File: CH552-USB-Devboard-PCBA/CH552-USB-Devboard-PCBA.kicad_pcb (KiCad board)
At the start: 2 copper layers, 22 x 48.1 mm, 47 parts, among them J1 Conn_01x11_Male, J2 Conn_01x11_Male, J3 USB_C_Receptacle, J4 USB_C_Receptacle, SW1 SW_Push, SW2 SW_Push, U2 CH552G, U3 TPS7A4101DGNT

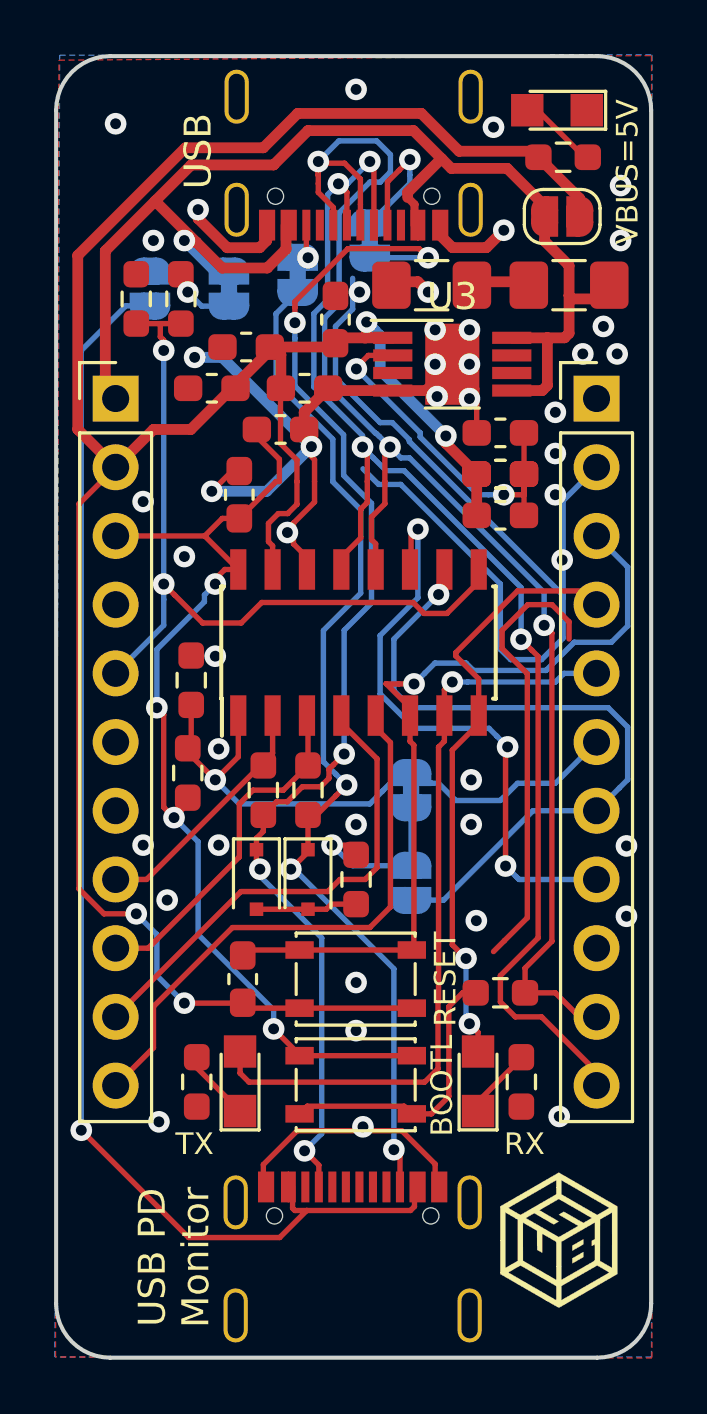
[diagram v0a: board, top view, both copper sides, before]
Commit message: create variant for PCBA
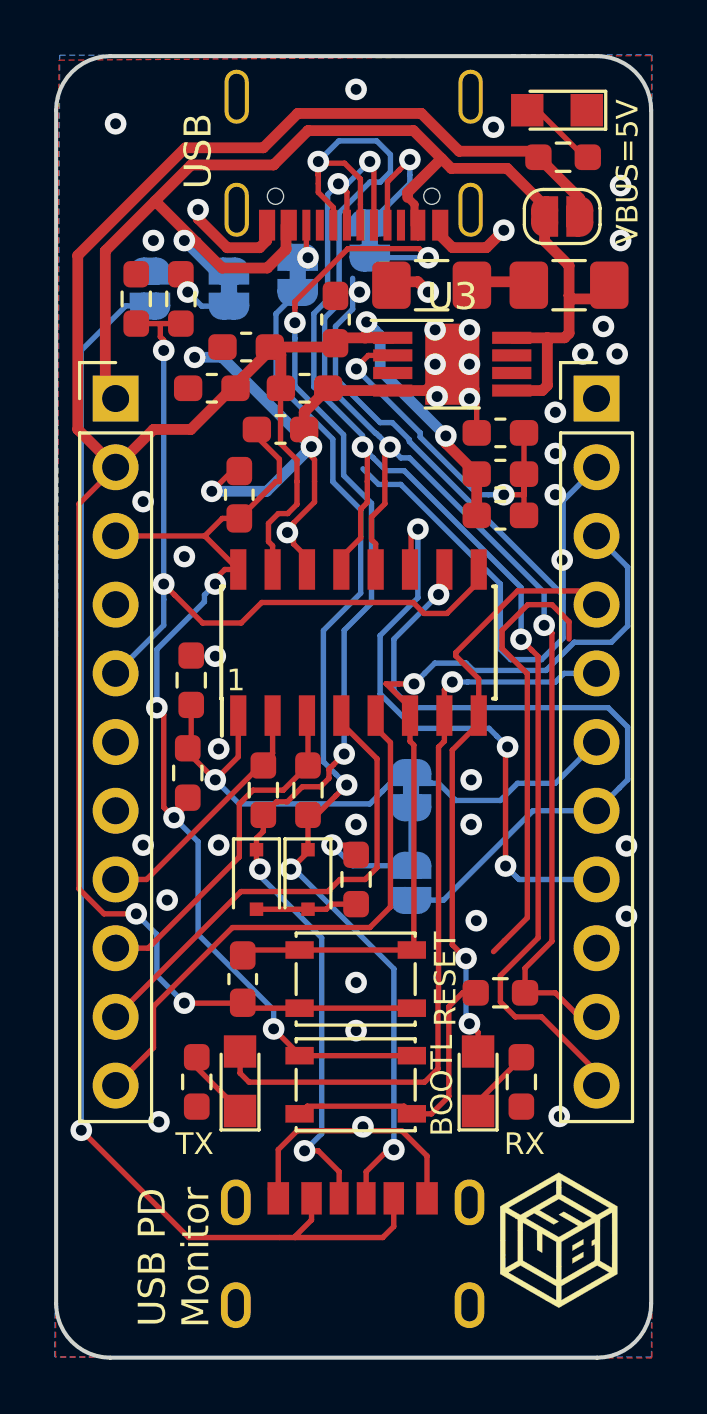
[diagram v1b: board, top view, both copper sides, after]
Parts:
- removed R14: DNP / 68k, Resistor_SMD:R_0603_1608Metric_Pad1.05x0.95mm_HandSolder
- J4: footprint footprint:VACON_CSP_USC16_TR -> CH552-USB-Devboard:Korean-Hroparts-Elec-TYPE-C-31-M-17
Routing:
- net /VBUS2: track 49.6 -> 48.5 mm
- net /CC1: track 45.8 -> 46.8 mm
- net /CC2: track 38.4 -> 39.3 mm
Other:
- board text added: "1"

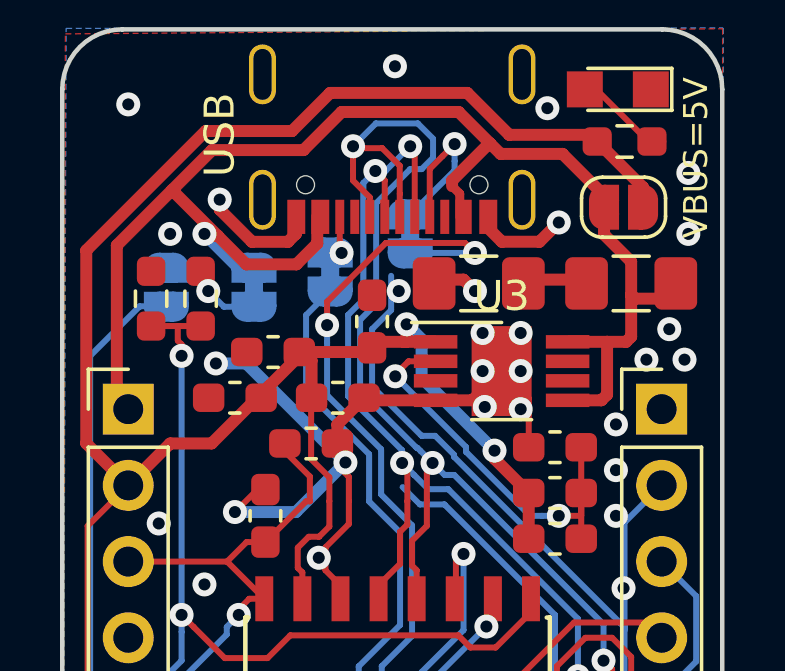
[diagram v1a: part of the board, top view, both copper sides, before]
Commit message: replace LDO
I'm quite sure it wasn't out of stock three days ago...
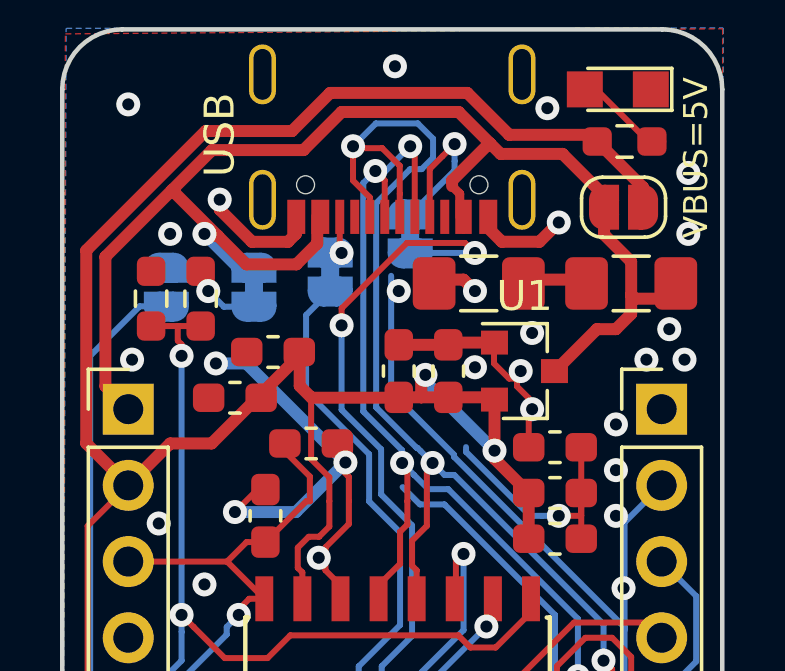
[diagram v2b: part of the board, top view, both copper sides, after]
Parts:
- removed U3: TPS7A4101DGNT, CH552-USB-Devboard:HVSSOP-8_3.0x3.0mm_P0.65mm
- added U1: ZXTR2105FQ, Package_TO_SOT_SMD:SOT-23, F.Cu at (89.4, 72.4)
- moved C9 3.03 mm to (86.9, 72.4)
- moved C10 2.22 mm to (85.2, 72.4), turned to 90 degrees
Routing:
- net Net-(C8-Pad2): track 13.6 -> 8.69 mm, vias 2 -> 1
- net GND: track 96.8 -> 93.7 mm, vias 45 -> 44
- net VBUS: track 50.1 -> 47.6 mm
- net VCC: track 93.5 -> 94.7 mm
- net /CC1: track 46.8 -> 46.0 mm
